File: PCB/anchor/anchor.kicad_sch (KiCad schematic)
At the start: 37 parts, among them J1 TSM-102-01-X-SV, J2 Conn_ARM_JTAG_SWD_10, J3 SM02B-SRSS-TB LFSN, J4 TSM-102-01-X-SV, J5 TSM-102-01-X-SV, J6 TSM-102-01-X-SV, J7 TSM-102-01-X-SV, J8 TSM-102-01-X-SV, Q1 IRLML2402TRPBF, Q2 IRLML2402TRPBF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

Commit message: update
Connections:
- net RX: now also U2.34 (P0.19/TX), U3.3 (RXD); no longer U2.32 (P0.15), U3.4 (TXD)
- net TX: now also U2.32 (P0.15/RX), U3.4 (TXD); no longer U2.34 (P0.19), U3.3 (RXD)
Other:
- moved on the sheet: U2
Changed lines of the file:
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@@
 		)
 	)
-	(label "TX"
+	(label "RX"
 		(at 373.38 153.67 90)
 		(fields_autoplaced yes)
@@
 		)
 	)
-	(label "RX"
+	(label "TX"
 		(at 215.9 146.05 180)
 		(fields_autoplaced yes)
@@
 		)
 	)
-	(label "TX"
+	(label "RX"
 		(at 215.9 140.97 180)
 		(fields_autoplaced yes)
@@
 		)
 	)
-	(label "RX"
+	(label "TX"
 		(at 375.92 153.67 90)
 		(fields_autoplaced yes)

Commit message: PCB updates
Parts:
- C1: now not fitted
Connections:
- net Vreg: no longer J1.02, J2.1 (VTref), J4.01, J7.01, J8.01, R5.1, R6.1
- net Vbatt+3.3V: now reaches J5.02, U1.1 (IN), U1.3 (EN)
- net RX renamed RX (BIDIRECTIONAL)
- net SWD_CLK renamed SWD_CLK (IN)
- net SWD_CLK (IN): no longer J2.4 (SWCLK/TCK)
- net SWD_DIO renamed SWD_DIO (BIDIRECTIONAL)
- net TX renamed TX (BIDIRECTIONAL)
- new net SWD_CLK (OUT): J2.4 (SWCLK/TCK)
- new net Vreg +3.3V: J1.02, J2.1 (VTref), J4.01, J7.01, J8.01, R5.1, R6.1
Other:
- company: (none) -> Team 3
- moved on the sheet: B1, B2, C2, C3, C4, C5, C6, C7, C8, D1, D2, D3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

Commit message: this is the newest folder status
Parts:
- removed J3: SM02B-SRSS-TB LFSN, Connector_JST:CONN_SM02B-SRSS-TB_JST, symbol SM02B-SRSS-TB:SM02B-SRSS-TB_LFSN
- added J3: S2B-PH-SM4-TB_LF__SN_, digikey-footprints:PinHeader_2x1mm_P2mm_SMD_RA, symbol dk_Rectangular-Connectors-Headers-Male-Pins:S2B-PH-SM4-TB_LF__SN_
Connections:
- net GND: now also J3.1
- net at J5.01, TP2.1: now also J3.2
- net RX (BIDIRECTIONAL) renamed LoRa RX (INPUT)
- net LoRa RX (INPUT): no longer U2.34 (P0.19/TX)
- net TX (BIDIRECTIONAL) renamed LoRa TX (INPUT)
- net LoRa TX (INPUT): no longer U3.4 (TXD)
- net Vbatt+3.3V renamed Vbatt +3.7V
- new net LoRa RX (OUTPUT): U2.34 (P0.19/TX)
- new net LoRa TX (OUTPUT): U3.4 (TXD)
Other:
- note added: "Power Inputs"
- note removed: "Vin and Voltage Regulator"
- moved on the sheet: TP2, TP3

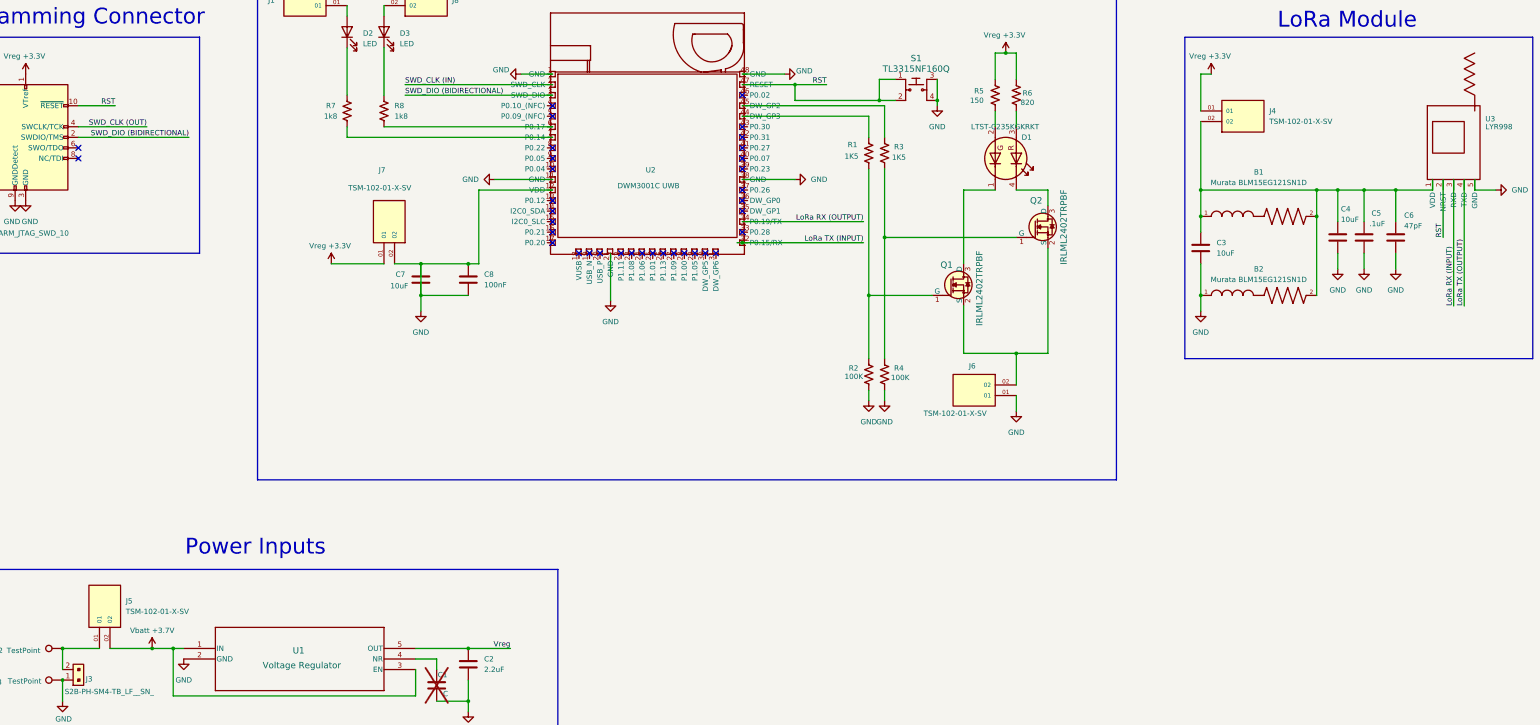
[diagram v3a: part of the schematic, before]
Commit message: added footprint folder and footprints to the cap's
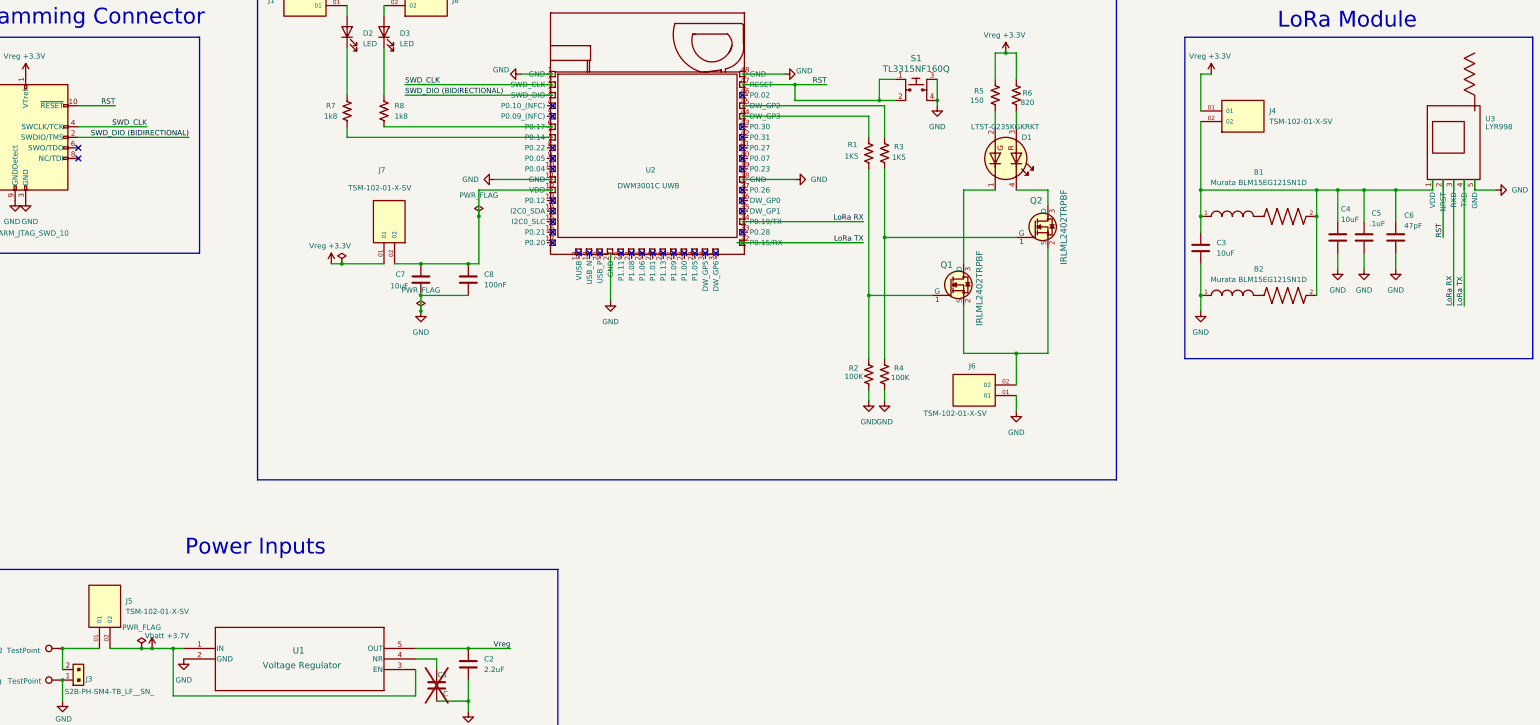
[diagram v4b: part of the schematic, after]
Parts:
- C2: footprint imported:GRM155C80J225KE95D -> GRM155C80J225KE95D:CAPC1005X55N
- C3, C4, C7: footprint (none) -> GRM155R60J106ME05D:CAPC1005X70N
- C5: footprint (none) -> GRM155R71C104KA88J:CAPC1005X55N
- C6: footprint (none) -> GRM1555C1H470JA01D:CAPC1005X55N
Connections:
- net LoRa RX (OUTPUT) is gone; now on net LoRa RX: U2.34 (P0.19/TX)
- net LoRa TX (OUTPUT) is gone; now on net LoRa TX: U3.4 (TXD)
- net SWD_CLK (OUT) is gone; now on net SWD_CLK: J2.4 (SWCLK/TCK)
- net GND: no longer C7.1, C8.1, J7.02, U2.12 (VDD)
- net LoRa RX (INPUT) renamed LoRa RX
- net LoRa TX (INPUT) renamed LoRa TX
- net SWD_CLK (IN) renamed SWD_CLK
- new net: C7.1, C8.1, J7.02, U2.12 (VDD)

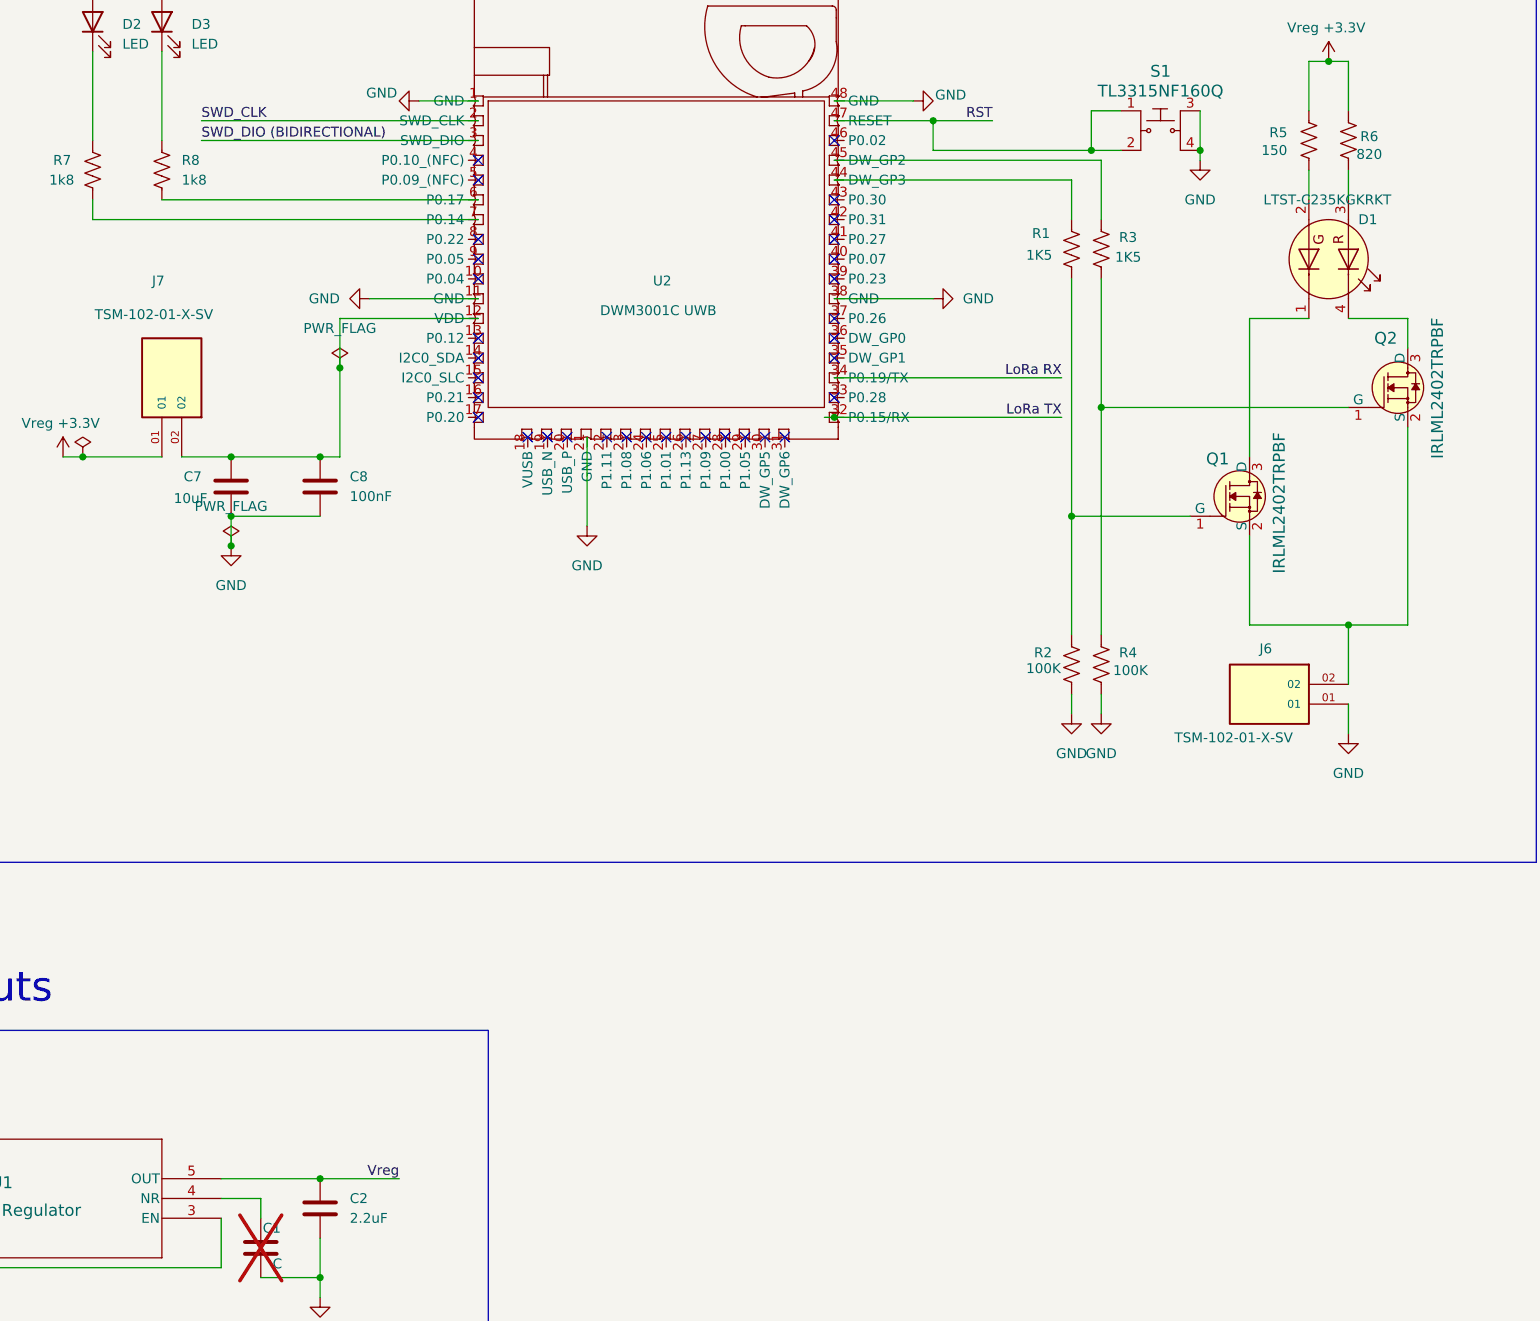
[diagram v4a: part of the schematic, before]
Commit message: updated pcb for anchor
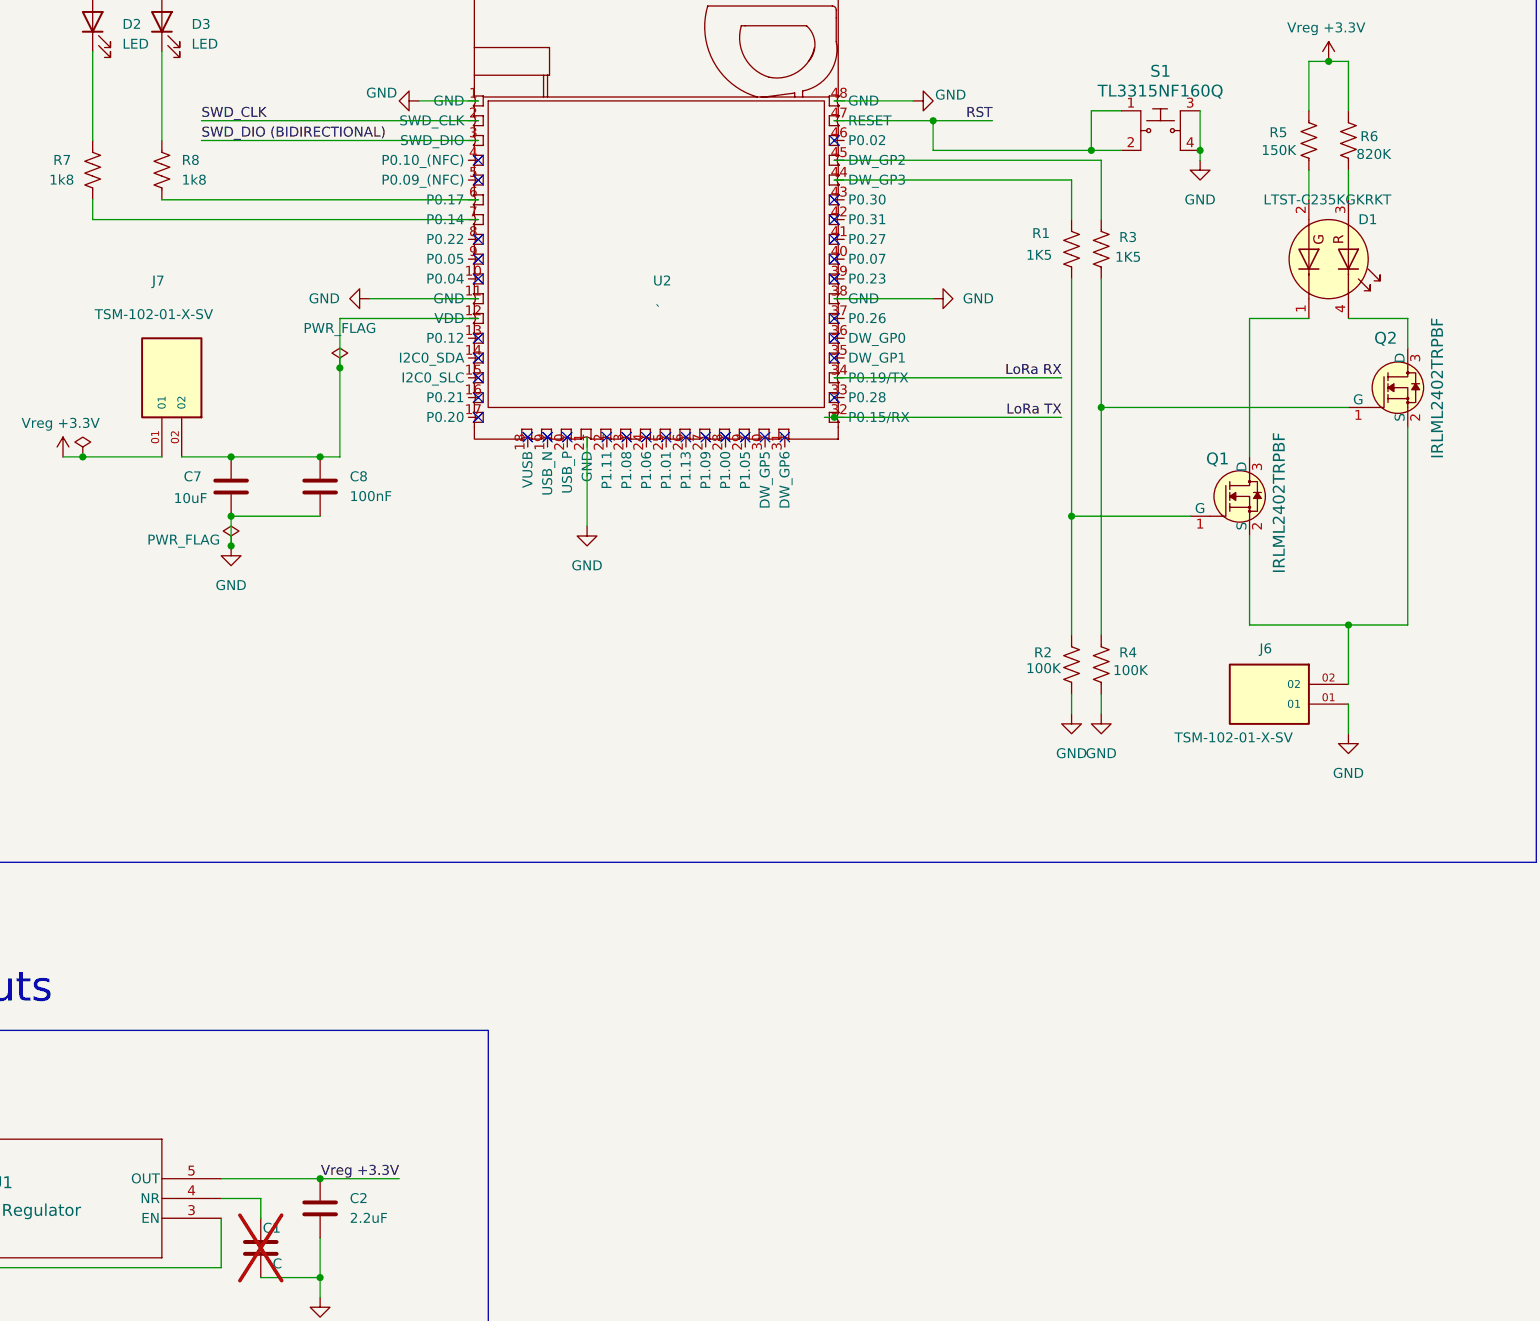
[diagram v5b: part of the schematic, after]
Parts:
- C1: footprint imported:GRM155C80J225KE95D -> GRM155C80J225KE95D:CAPC1005X55N
- C8: footprint (none) -> Capacitor_SMD:C_0201_0603Metric
- D1: footprint LED_SMD:LED_LiteOn_LTST-C235KGKRKT -> APHBM2012LSURKSYKC:LED_APHBM2012LSURKSYKC
- D2, D3: footprint (none) -> 150060RS75000:WL-SMCW_0603
- J1, J4, J5, J6, J7, J8: footprint TSM-102-01-X-SV:SAMTEC_TSM-102-01-X-SV -> TSM_102_01_L_SV:SAMTEC_TSM-102-01-X-SV
- J3: footprint digikey-footprints:PinHeader_2x1mm_P2mm_SMD_RA -> S2B_PH_SM4_TB:JST_S2B-PH-SM4-TB
- Q1, Q2: footprint digikey-footprints:SOT-23-3 -> Package_TO_SOT_SMD:SOT-23-3
- R1, R3: footprint (none) -> RT0402BRD071K5L:RESC1005X35N
- R2, R4: footprint (none) -> RC0402FR_07100KL:RESC1005X40
- R5: value 150 -> 150K; footprint (none) -> RC0402FR_07150RL:RESC1005X40N
- R6: value 820 -> 820K; footprint (none) -> RC0402FR_07820KL:RESC1005X40N
- R7, R8: footprint (none) -> RK73B1ETTP182J:RESC1005X40N
- S1: footprint digikey-footprints:Switch_Tactile_SMD_4.5x4.5mm_TL3315NF160Q -> TL3315NF160Q:SW_TL3315NF160Q
- TP2, TP3: footprint (none) -> TestPoint:TestPoint_Keystone_5015_Micro-Minature
- U1: footprint Package_TO_SOT_SMD:DDC5 -> TPS79933DDCR (2):volt_reg
- U2: value DWM3001C UWB -> `; footprint DWM3001C:DWM3001C -> Altium:DWM3001C
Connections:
- net Vreg is gone; now on net Vreg +3.3V: C2.2, U1.5 (OUT)
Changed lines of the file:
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@@
 		)
 	)
-	(label "Vreg"
+	(label "Vreg +3.3V"
 		(at 158.75 228.6 180)
 		(fields_autoplaced yes)
@@
 			)
 		)
-		(property "Footprint" ""
+		(property "Footprint" "150060RS75000:WL-SMCW_0603"
 			(at 128.27 80.01 0)
 			(effects
@@
 			)
 		)
-		(property "Footprint" ""
+		(property "Footprint" "RC0402FR_07100KL:RESC1005X40"
 			(at 249.936 162.814 90)
 			(effects
@@
 			)
 		)
-		(property "Footprint" "LED_SMD:LED_LiteOn_LTST-C235KGKRKT"
+		(property "Footprint" "APHBM2012LSURKSYKC:LED_APHBM2012LSURKSYKC"
 			(at 278.13 111.252 0)
 			(effects
@@
 			)
 		)
-		(property "Value" "DWM3001C UWB"
+		(property "Value" "`"
 			(at 192.024 117.094 0)
 			(effects
@@
 			)
 		)
-		(property "Footprint" "DWM3001C:DWM3001C"
+		(property "Footprint" "Altium:DWM3001C"
 			(at 190.5 112.268 0)
 			(effects
@@
 		(on_board yes)
 		(dnp no)
-		(fields_autoplaced yes)
 		(property "Reference" "#FLG04"
 			(at 137.16 145.415 0)
@@
 		)
 		(property "Value" "PWR_FLAG"
-			(at 137.16 142.24 0)
+			(at 131.064 146.558 0)
 			(effects
 				(font
@@
 			)
 		)
-		(property "Footprint" "digikey-footprints:SOT-23-3"
+		(property "Footprint" "Package_TO_SOT_SMD:SOT-23-3"
 			(at 273.05 135.89 0)
 			(effects
@@
 			)
 		)
-		(property "Footprint" ""
+		(property "Footprint" "RK73B1ETTP182J:RESC1005X40N"
 			(at 120.396 99.314 90)
 			(effects
@@
 			)
 		)
-		(property "Footprint" "digikey-footprints:Switch_Tactile_SMD_4.5x4.5mm_TL3315NF160Q"
+		(property "Footprint" "TL3315NF160Q:SW_TL3315NF160Q"
 			(at 261.62 88.9 0)
 			(effects
@@
 			)
 		)
-		(property "Value" "150"
+		(property "Value" "150K"
 			(at 269.494 96.52 0)
 			(effects
@@
 			)
 		)
-		(property "Footprint" ""
+		(property "Footprint" "RC0402FR_07150RL:RESC1005X40N"
 			(at 276.606 95.504 90)
 			(effects
@@
 			)
 		)
-		(property "Footprint" ""
+		(property "Footprint" "150060RS75000:WL-SMCW_0603"
 			(at 119.38 80.01 0)
 			(effects
@@
 			)
 		)
-		(property "Footprint" "digikey-footprints:PinHeader_2x1mm_P2mm_SMD_RA"
+		(property "Footprint" "S2B_PH_SM4_TB:JST_S2B-PH-SM4-TB"
 			(at 48.26 231.14 0)
 			(effects
@@
 			)
 		)
-		(property "Footprint" ""
+		(property "Footprint" "RT0402BRD071K5L:RESC1005X35N"
 			(at 246.126 109.474 90)
 			(effects
@@
 			)
 		)
-		(property "Footprint" ""
+		(property "Footprint" "RC0402FR_07100KL:RESC1005X40"
 			(at 246.126 162.814 90)
 			(effects
@@
 			)
 		)
-		(property "Footprint" ""
+		(property "Footprint" "Capacitor_SMD:C_0201_0603Metric"
 			(at 149.5552 143.51 0)
 			(effects
@@
 			)
 		)
-		(property "Footprint" ""
+		(property "Footprint" "RT0402BRD071K5L:RESC1005X35N"
 			(at 249.936 109.474 90)
 			(effects
@@
 			)
 		)
-		(property "Footprint" "TSM-102-01-X-SV:SAMTEC_TSM-102-01-X-SV"
+		(property "Footprint" "TSM_102_01_L_SV:SAMTEC_TSM-102-01-X-SV"
 			(at 138.176 66.294 0)
 			(effects
@@
 			)
 		)
-		(property "Footprint" "Package_TO_SOT_SMD:DDC5"
+		(property "Footprint" "TPS79933DDCR (2):volt_reg"
 			(at 80.01 228.6 0)
 			(effects
@@
 			)
 		)
-		(property "Footprint" "TSM-102-01-X-SV:SAMTEC_TSM-102-01-X-SV"
+		(property "Footprint" "TSM_102_01_L_SV:SAMTEC_TSM-102-01-X-SV"
 			(at 109.474 78.486 0)
 			(effects
@@
 			)
 		)
-		(property "Footprint" "TSM-102-01-X-SV:SAMTEC_TSM-102-01-X-SV"
+		(property "Footprint" "TSM_102_01_L_SV:SAMTEC_TSM-102-01-X-SV"
 			(at 270.764 172.466 0)
 			(effects
@@
 			)
 		)
-		(property "Footprint" "TSM-102-01-X-SV:SAMTEC_TSM-102-01-X-SV"
+		(property "Footprint" "TSM_102_01_L_SV:SAMTEC_TSM-102-01-X-SV"
 			(at 335.026 94.234 0)
 			(effects
@@
 			)
 		)
-		(property "Footprint" ""
+		(property "Footprint" "RK73B1ETTP182J:RESC1005X40N"
 			(at 129.286 99.314 90)
 			(effects
@@
 			)
 		)
-		(property "Footprint" ""
+		(property "Footprint" "TestPoint:TestPoint_Keystone_5015_Micro-Minature"
 			(at 50.8 223.52 0)
 			(effects
@@
 			)
 		)
-		(property "Footprint" "TSM-102-01-X-SV:SAMTEC_TSM-102-01-X-SV"
+		(property "Footprint" "TSM_102_01_L_SV:SAMTEC_TSM-102-01-X-SV"
 			(at 123.444 125.984 0)
 			(effects
@@
 			)
 		)
-		(property "Footprint" ""
+		(property "Footprint" "TestPoint:TestPoint_Keystone_5015_Micro-Minature"
 			(at 50.8 231.14 0)
 			(effects
@@
 			)
 		)
-		(property "Footprint" "TSM-102-01-X-SV:SAMTEC_TSM-102-01-X-SV"
+		(property "Footprint" "TSM_102_01_L_SV:SAMTEC_TSM-102-01-X-SV"
 			(at 54.864 218.694 0)
 			(effects
@@
 			)
 		)
-		(property "Footprint" "digikey-footprints:SOT-23-3"
+		(property "Footprint" "Package_TO_SOT_SMD:SOT-23-3"
 			(at 293.37 121.92 0)
 			(effects
@@
 			)
 		)
-		(property "Value" "820"
+		(property "Value" "820K"
 			(at 281.686 97.028 0)
 			(effects
@@
 			)
 		)
-		(property "Footprint" ""
+		(property "Footprint" "RC0402FR_07820KL:RESC1005X40N"
 			(at 281.686 95.504 90)
 			(effects
@@
 			)
 		)
-		(property "Footprint" "imported:GRM155C80J225KE95D"
+		(property "Footprint" "GRM155C80J225KE95D:CAPC1005X55N"
 			(at 141.9352 241.3 0)
 			(effects
